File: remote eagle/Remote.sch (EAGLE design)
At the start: 13 parts, among them Y1 8MHz

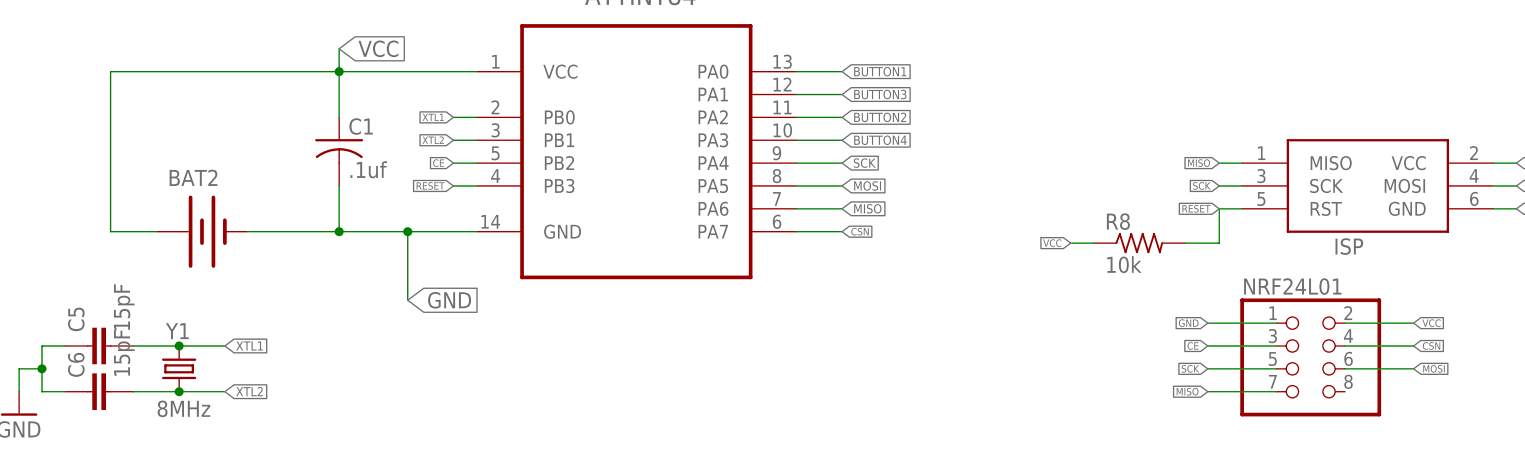
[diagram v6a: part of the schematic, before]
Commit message: Re-laying out the board for the third revision. This one has correct wiring, less expensive crystal, and components in more logical places. Could use some contact points.
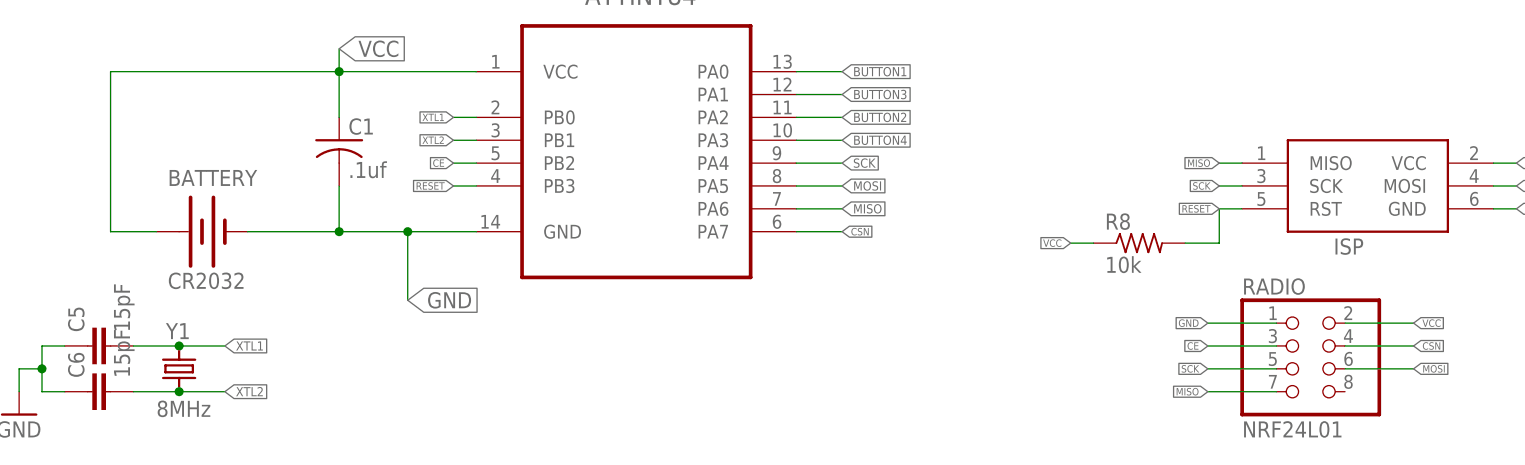
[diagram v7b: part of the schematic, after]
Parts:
- BATTERY: value (none) -> CR2032
- RADIO: value (none) -> NRF24L01
- Y1: device SparkFun:CRYSTAL5X3 -> remote:CRYSTAL
- renumbered BAT2 to BATTERY, NRF24L01 to RADIO
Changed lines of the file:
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@@
 <part name="C1" library="adafruit" deviceset="C-US" device="C0805" value=".1uf"/>
 <part name="ISP" library="adafruit" deviceset="AVRISP" device="-6"/>
-<part name="NRF24L01" library="pinhead" deviceset="PINHD-2X4" device=""/>
+<part name="RADIO" library="pinhead" deviceset="PINHD-2X4" device="" value="NRF24L01"/>
 <part name="R8" library="adafruit" deviceset="R-US_" device="R0805" value="10k"/>
-<part name="Y1" library="SparkFun" deviceset="CRYSTAL" device="5X3" value="8MHz"/>
+<part name="Y1" library="remote" deviceset="CRYSTAL" device="" value="8MHz"/>
 <part name="GND3" library="SparkFun" deviceset="GND" device=""/>
-<part name="BAT2" library="SparkFun-Electromechanical" deviceset="BATTERY" device="20MM_4LEGS_OVERPASTE"/>
+<part name="BATTERY" library="SparkFun-Electromechanical" deviceset="BATTERY" device="20MM_4LEGS_OVERPASTE" value="CR2032"/>
 <part name="C5" library="SparkFun-Passives" deviceset="CAP" device="0805" value="15pF"/>
 <part name="C6" library="SparkFun-Passives" deviceset="CAP" device="0805" value="15pF"/>
@@
 <instance part="C1" gate="G$1" x="43.18" y="20.32"/>
 <instance part="ISP" gate="G$1" x="156.21" y="15.24"/>
-<instance part="NRF24L01" gate="A" x="149.86" y="-5.08"/>
+<instance part="RADIO" gate="A" x="149.86" y="-5.08"/>
 <instance part="R8" gate="G$1" x="132.08" y="8.89"/>
 <instance part="Y1" gate="G$1" x="25.4" y="-5.08" smashed="yes" rot="R90">
@@
 </instance>
 <instance part="GND3" gate="1" x="7.62" y="-10.16"/>
-<instance part="BAT2" gate="G$1" x="27.94" y="10.16"/>
+<instance part="BATTERY" gate="G$1" x="27.94" y="10.16"/>
 <instance part="C5" gate="G$1" x="17.78" y="-2.54" rot="R90"/>
 <instance part="C6" gate="G$1" x="17.78" y="-7.62" rot="R90"/>
@@
 <wire x1="33.02" y1="10.16" x2="43.18" y2="10.16" width="0.1524" layer="91"/>
 <junction x="43.18" y="10.16"/>
-<pinref part="BAT2" gate="G$1" pin="-"/>
+<pinref part="BATTERY" gate="G$1" pin="-"/>
 </segment>
 <segment>
@@
 </segment>
 <segment>
-<pinref part="NRF24L01" gate="A" pin="1"/>
+<pinref part="RADIO" gate="A" pin="1"/>
 <wire x1="147.32" y1="0" x2="139.7" y2="0" width="0.1524" layer="91"/>
 <label x="139.7" y="0" size="0.8128" layer="95" rot="R180" xref="yes"/>
@@
 <wire x1="147.32" y1="-7.62" x2="139.7" y2="-7.62" width="0.1524" layer="91"/>
 <label x="139.7" y="-7.62" size="0.8128" layer="95" rot="R180" xref="yes"/>
-<pinref part="NRF24L01" gate="A" pin="7"/>
+<pinref part="RADIO" gate="A" pin="7"/>
 </segment>
 <segment>
@@
 <wire x1="154.94" y1="-5.08" x2="162.56" y2="-5.08" width="0.1524" layer="91"/>
 <label x="162.56" y="-5.08" size="0.8128" layer="95" xref="yes"/>
-<pinref part="NRF24L01" gate="A" pin="6"/>
+<pinref part="RADIO" gate="A" pin="6"/>
 </segment>
 <segment>
@@
 <segment>
 <label x="139.7" y="-5.08" size="0.8128" layer="95" rot="R180" xref="yes"/>
-<pinref part="NRF24L01" gate="A" pin="5"/>
+<pinref part="RADIO" gate="A" pin="5"/>
 <wire x1="139.7" y1="-5.08" x2="147.32" y2="-5.08" width="0.1524" layer="91"/>
 </segment>
@@
 <wire x1="17.78" y1="27.94" x2="17.78" y2="10.16" width="0.1524" layer="91"/>
 <wire x1="17.78" y1="10.16" x2="22.86" y2="10.16" width="0.1524" layer="91"/>
-<pinref part="BAT2" gate="G$1" pin="+"/>
+<pinref part="BATTERY" gate="G$1" pin="+"/>
 </segment>
 <segment>
@@
 </segment>
 <segment>
-<pinref part="NRF24L01" gate="A" pin="2"/>
+<pinref part="RADIO" gate="A" pin="2"/>
 <wire x1="154.94" y1="0" x2="162.56" y2="0" width="0.1524" layer="91"/>
 <label x="162.56" y="0" size="0.8128" layer="95" xref="yes"/>
@@
 <net name="CE" class="0">
 <segment>
-<pinref part="NRF24L01" gate="A" pin="3"/>
+<pinref part="RADIO" gate="A" pin="3"/>
 <wire x1="147.32" y1="-2.54" x2="139.7" y2="-2.54" width="0.1524" layer="91"/>
 <label x="139.7" y="-2.54" size="0.8128" layer="95" rot="R180" xref="yes"/>
@@
 <net name="CSN" class="0">
 <segment>
-<pinref part="NRF24L01" gate="A" pin="4"/>
+<pinref part="RADIO" gate="A" pin="4"/>
 <wire x1="154.94" y1="-2.54" x2="162.56" y2="-2.54" width="0.1524" layer="91"/>
 <label x="162.56" y="-2.54" size="0.8128" layer="95" xref="yes"/>
@@
 </sheet>
 </sheets>
+<errors>
+</errors>
 </schematic>
 </drawing>

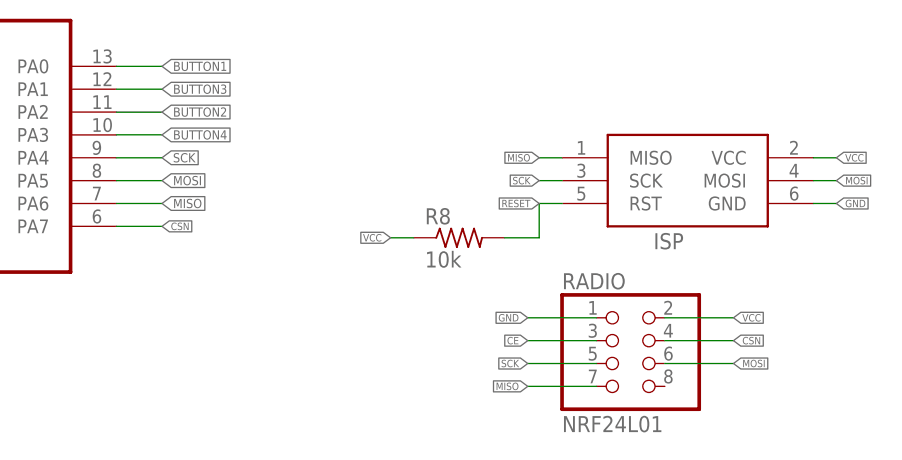
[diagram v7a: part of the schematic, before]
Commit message: Swapping MOSI/MISO on radio, isp, and mcu.
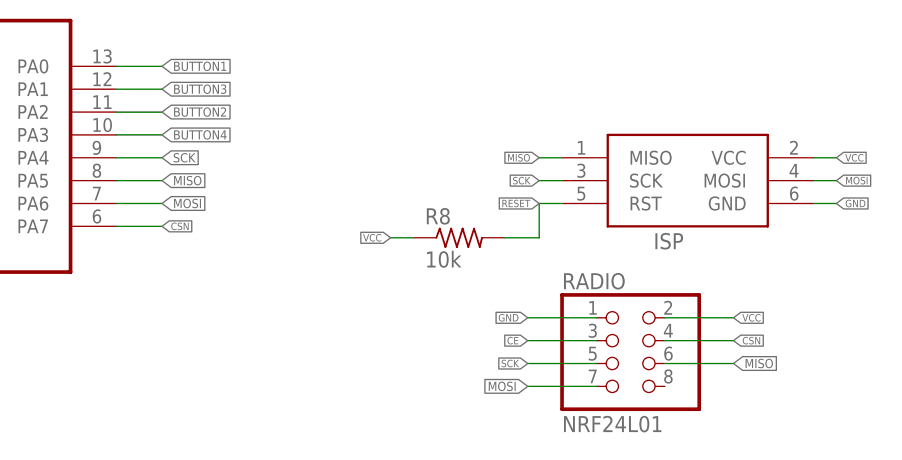
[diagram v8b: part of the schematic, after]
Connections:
- net MISO: now also ATTINY84.PA5, RADIO.6; no longer ATTINY84.PA6, RADIO.7
- net MOSI: now also ATTINY84.PA6, RADIO.7; no longer ATTINY84.PA5, RADIO.6
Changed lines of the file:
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@@
 </segment>
 <segment>
-<wire x1="147.32" y1="-7.62" x2="139.7" y2="-7.62" width="0.1524" layer="91"/>
-<label x="139.7" y="-7.62" size="0.8128" layer="95" rot="R180" xref="yes"/>
-<pinref part="RADIO" gate="A" pin="7"/>
+<pinref part="RADIO" gate="A" pin="6"/>
+<wire x1="154.94" y1="-5.08" x2="162.56" y2="-5.08" width="0.1524" layer="91"/>
+<label x="162.56" y="-5.08" size="1.016" layer="95" xref="yes"/>
 </segment>
 <segment>
-<pinref part="ATTINY84" gate="A" pin="PA6"/>
-<wire x1="93.98" y1="12.7" x2="99.06" y2="12.7" width="0.1524" layer="91"/>
-<label x="99.06" y="12.7" size="1.016" layer="95" font="vector" xref="yes"/>
+<pinref part="ATTINY84" gate="A" pin="PA5"/>
+<wire x1="93.98" y1="15.24" x2="99.06" y2="15.24" width="0.1524" layer="91"/>
+<label x="99.06" y="15.24" size="1.016" layer="95" xref="yes"/>
 </segment>
 </net>
@@
 </segment>
 <segment>
-<wire x1="154.94" y1="-5.08" x2="162.56" y2="-5.08" width="0.1524" layer="91"/>
-<label x="162.56" y="-5.08" size="0.8128" layer="95" xref="yes"/>
-<pinref part="RADIO" gate="A" pin="6"/>
+<pinref part="RADIO" gate="A" pin="7"/>
+<wire x1="147.32" y1="-7.62" x2="139.7" y2="-7.62" width="0.1524" layer="91"/>
+<label x="139.7" y="-7.62" size="1.016" layer="95" font="vector" rot="R180" xref="yes"/>
 </segment>
 <segment>
-<pinref part="ATTINY84" gate="A" pin="PA5"/>
-<wire x1="93.98" y1="15.24" x2="99.06" y2="15.24" width="0.1524" layer="91"/>
-<label x="99.06" y="15.24" size="1.016" layer="95" font="vector" xref="yes"/>
+<pinref part="ATTINY84" gate="A" pin="PA6"/>
+<wire x1="93.98" y1="12.7" x2="99.06" y2="12.7" width="0.1524" layer="91"/>
+<label x="99.06" y="12.7" size="1.016" layer="95" xref="yes"/>
 </segment>
 </net>
